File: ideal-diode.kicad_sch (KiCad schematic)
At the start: 4 parts, among them Q2 SQS401EN-T1_BE3, U11 LTC4412IS6

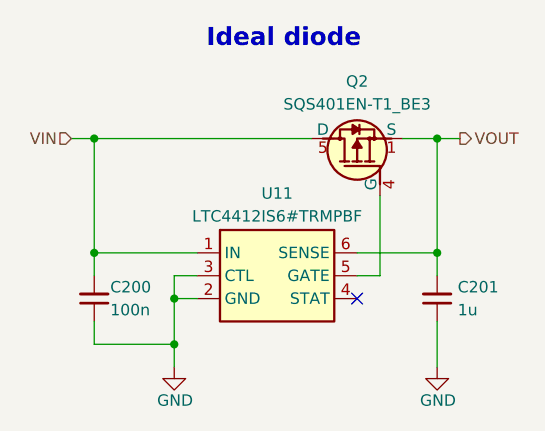
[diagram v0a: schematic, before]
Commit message: [#86617] Unify captions, add TVS to USB VBUS
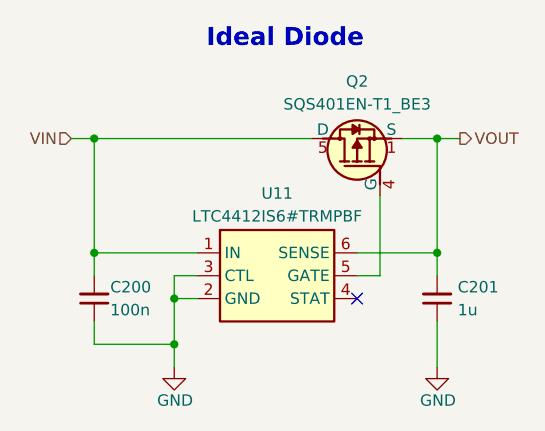
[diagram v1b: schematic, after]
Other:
- note added: "Ideal Diode"
- note removed: "Ideal diode"
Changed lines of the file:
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@@
 		(comment 1 "www.antmicro.com")
 	)
-	(text "Ideal diode"
+	(text "Ideal Diode"
 		(exclude_from_sim no)
 		(at 200.406 127.254 0)

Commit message: [#86351] Rename project
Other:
- title: 10GbE Expansion -> OCuLink to 10GbE adapter
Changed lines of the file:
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@@
 	(paper "A3")
 	(title_block
-		(title "10GbE Expansion")
+		(title "OCuLink to 10GbE adapter")
 		(date "2025-11-07")
 		(rev "1.0.0")
@@
 		)
 		(instances
-			(project "10-gbe-expansion"
+			(project "OCuLink to 10GbE adapter"
 				(path "/04bda987-e5eb-48b4-9e90-d8211dc11b39/3d913a88-b6f3-4148-9b3d-882d5df37282/151969d2-a4e0-4623-bed4-6527ef713b4c"
 					(reference "C203")
@@
 		)
 		(instances
-			(project "10-gbe-expansion"
+			(project "OCuLink to 10GbE adapter"
 				(path "/04bda987-e5eb-48b4-9e90-d8211dc11b39/3d913a88-b6f3-4148-9b3d-882d5df37282/151969d2-a4e0-4623-bed4-6527ef713b4c"
 					(reference "C202")
@@
 		)
 		(instances
-			(project "10-gbe-expansion"
+			(project "OCuLink to 10GbE adapter"
 				(path "/04bda987-e5eb-48b4-9e90-d8211dc11b39/3d913a88-b6f3-4148-9b3d-882d5df37282/151969d2-a4e0-4623-bed4-6527ef713b4c"
 					(reference "#PWR0330")
@@
 		)
 		(instances
-			(project "10-gbe-expansion"
+			(project "OCuLink to 10GbE adapter"
 				(path "/04bda987-e5eb-48b4-9e90-d8211dc11b39/3d913a88-b6f3-4148-9b3d-882d5df37282/151969d2-a4e0-4623-bed4-6527ef713b4c"
 					(reference "#PWR0331")
@@
 		)
 		(instances
-			(project "10-gbe-expansion"
+			(project "OCuLink to 10GbE adapter"
 				(path "/04bda987-e5eb-48b4-9e90-d8211dc11b39/3d913a88-b6f3-4148-9b3d-882d5df37282/151969d2-a4e0-4623-bed4-6527ef713b4c"
 					(reference "U12")
@@
 		)
 		(instances
-			(project "10-gbe-expansion"
+			(project "OCuLink to 10GbE adapter"
 				(path "/04bda987-e5eb-48b4-9e90-d8211dc11b39/3d913a88-b6f3-4148-9b3d-882d5df37282/151969d2-a4e0-4623-bed4-6527ef713b4c"
 					(reference "Q3")
